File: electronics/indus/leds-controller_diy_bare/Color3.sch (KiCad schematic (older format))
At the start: 14 parts

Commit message: wip bare diy controller - dcdc and refactor
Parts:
- gave numbers to parts that had none: 14
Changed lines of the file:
@@
 $Descr A4 11693 8268
 encoding utf-8
-Sheet 5 8
+Sheet 5 9
 Title "Carte controlleur de LEDs 4 canaux"
 Date ""
@@
 VIN_24V
 $Comp
-L TPS92513 U?
+L TPS92513 U5
 U 1 1 5715946D
 P 5850 3550
-F 0 "U?" H 6200 2600 60  0000 C CNN
+F 0 "U5" H 6200 2600 60  0000 C CNN
 F 1 "TPS92513" H 5450 2600 60  0000 C CNN
 F 2 "" H 6000 3650 60  0000 C CNN
@@
 	1150 3450 5300 3450
 $Comp
-L GND-RESCUE-leds-controller #PWR?
+L GND-RESCUE-leds-controller #PWR020
 U 1 1 57159475
 P 3400 3100
-F 0 "#PWR?" H 3400 3100 30  0001 C CNN
+F 0 "#PWR020" H 3400 3100 30  0001 C CNN
 F 1 "GND" H 3400 3030 30  0001 C CNN
 F 2 "" H 3400 3100 60  0000 C CNN
@@
 $EndComp
 $Comp
-L C-RESCUE-leds-controller C?
+L C-RESCUE-leds-controller C20
 U 1 1 5715947B
 P 3400 2650
-F 0 "C?" H 3400 2750 40  0000 L CNN
+F 0 "C20" H 3400 2750 40  0000 L CNN
 F 1 "C" H 3406 2565 40  0000 L CNN
 F 2 "" H 3438 2500 30  0000 C CNN
@@
 $EndComp
 $Comp
-L R-RESCUE-leds-controller R?
+L R-RESCUE-leds-controller R23
 U 1 1 57159482
 P 4150 2700
-F 0 "R?" V 4230 2700 40  0000 C CNN
+F 0 "R23" V 4230 2700 40  0000 C CNN
 F 1 "R" V 4157 2701 40  0000 C CNN
 F 2 "" V 4080 2700 30  0000 C CNN
@@
 Connection ~ 4150 3450
 $Comp
-L C-RESCUE-leds-controller C?
+L C-RESCUE-leds-controller C18
 U 1 1 5715948C
 P 1650 4150
-F 0 "C?" H 1650 4250 40  0000 L CNN
+F 0 "C18" H 1650 4250 40  0000 L CNN
 F 1 "C" H 1656 4065 40  0000 L CNN
 F 2 "" H 1688 4000 30  0000 C CNN
@@
 Connection ~ 5800 4900
 $Comp
-L GND-RESCUE-leds-controller #PWR?
+L GND-RESCUE-leds-controller #PWR021
 U 1 1 5715949A
 P 6000 5250
-F 0 "#PWR?" H 6000 5250 30  0001 C CNN
+F 0 "#PWR021" H 6000 5250 30  0001 C CNN
 F 1 "GND" H 6000 5180 30  0001 C CNN
 F 2 "" H 6000 5250 60  0000 C CNN
@@
 Connection ~ 6000 4900
 $Comp
-L R-RESCUE-leds-controller R?
+L R-RESCUE-leds-controller R20
 U 1 1 571594A1
 P 2200 3800
-F 0 "R?" V 2280 3800 40  0000 C CNN
+F 0 "R20" V 2280 3800 40  0000 C CNN
 F 1 "R" V 2207 3801 40  0000 C CNN
 F 2 "" V 2130 3800 30  0000 C CNN
@@
 $EndComp
 $Comp
-L R-RESCUE-leds-controller R?
+L R-RESCUE-leds-controller R21
 U 1 1 571594A8
 P 2200 4500
-F 0 "R?" V 2280 4500 40  0000 C CNN
+F 0 "R21" V 2280 4500 40  0000 C CNN
 F 1 "R" V 2207 4501 40  0000 C CNN
 F 2 "" V 2130 4500 30  0000 C CNN
@@
 Connection ~ 2200 4150
 $Comp
-L C-RESCUE-leds-controller C?
+L C-RESCUE-leds-controller C19
 U 1 1 571594B8
 P 3100 4300
-F 0 "C?" H 3100 4400 40  0000 L CNN
+F 0 "C19" H 3100 4400 40  0000 L CNN
 F 1 "C" H 3106 4215 40  0000 L CNN
 F 2 "" H 3138 4150 30  0000 C CNN
@@
 $EndComp
 $Comp
-L R-RESCUE-leds-controller R?
+L R-RESCUE-leds-controller R22
 U 1 1 571594BF
 P 4100 4500
-F 0 "R?" V 4180 4500 40  0000 C CNN
+F 0 "R22" V 4180 4500 40  0000 C CNN
 F 1 "R" V 4107 4501 40  0000 C CNN
 F 2 "" V 4030 4500 30  0000 C CNN
@@
 Connection ~ 4100 4900
 $Comp
-L INDUCTOR L?
+L INDUCTOR L4
 U 1 1 571594CE
 P 8250 3450
-F 0 "L?" V 8200 3450 40  0000 C CNN
+F 0 "L4" V 8200 3450 40  0000 C CNN
 F 1 "XAL6060-153MEC - 15µH - 6A" V 8350 3450 40  0000 C CNN
 F 2 "risebox:SELF_COILCRAFT_XAL6060-153" H 8250 3450 60  0001 C CNN
@@
 	6050 2950 6050 2250
 $Comp
-L C-RESCUE-leds-controller C?
+L C-RESCUE-leds-controller C21
 U 1 1 571594DE
 P 6850 2900
-F 0 "C?" H 6850 3000 40  0000 L CNN
+F 0 "C21" H 6850 3000 40  0000 L CNN
 F 1 "C" H 6856 2815 40  0000 L CNN
 F 2 "" H 6888 2750 30  0000 C CNN
@@
 	8550 3450 10500 3450
 $Comp
-L C-RESCUE-leds-controller C?
+L C-RESCUE-leds-controller C22
 U 1 1 571594EF
 P 9600 3750
-F 0 "C?" H 9600 3850 40  0000 L CNN
+F 0 "C22" H 9600 3850 40  0000 L CNN
 F 1 "C" H 9606 3665 40  0000 L CNN
 F 2 "" H 9638 3600 30  0000 C CNN
@@
 Connection ~ 9600 4050
 $Comp
-L R-RESCUE-leds-controller R?
+L R-RESCUE-leds-controller R24
 U 1 1 571594FA
 P 8250 4050
-F 0 "R?" V 8330 4050 40  0000 C CNN
+F 0 "R24" V 8330 4050 40  0000 C CNN
 F 1 "R" V 8257 4051 40  0000 C CNN
 F 2 "" V 8180 4050 30  0000 C CNN
@@
 	8500 4050 10500 4050
 $Comp
-L R-RESCUE-leds-controller R?
+L R-RESCUE-leds-controller R25
 U 1 1 57159503
 P 10200 4500
-F 0 "R?" V 10280 4500 40  0000 C CNN
+F 0 "R25" V 10280 4500 40  0000 C CNN
 F 1 "R" V 10207 4501 40  0000 C CNN
 F 2 "" V 10130 4500 30  0000 C CNN
@@
 	10200 4900 10200 4750
 $Comp
-L DIODESCH D?
+L DIODESCH D5
 U 1 1 5715950D
 P 7400 4500
-F 0 "D?" H 7400 4600 40  0000 C CNN
+F 0 "D5" H 7400 4600 40  0000 C CNN
 F 1 "DIODESCH" H 7400 4400 40  0000 C CNN
 F 2 "" H 7400 4500 60  0000 C CNN

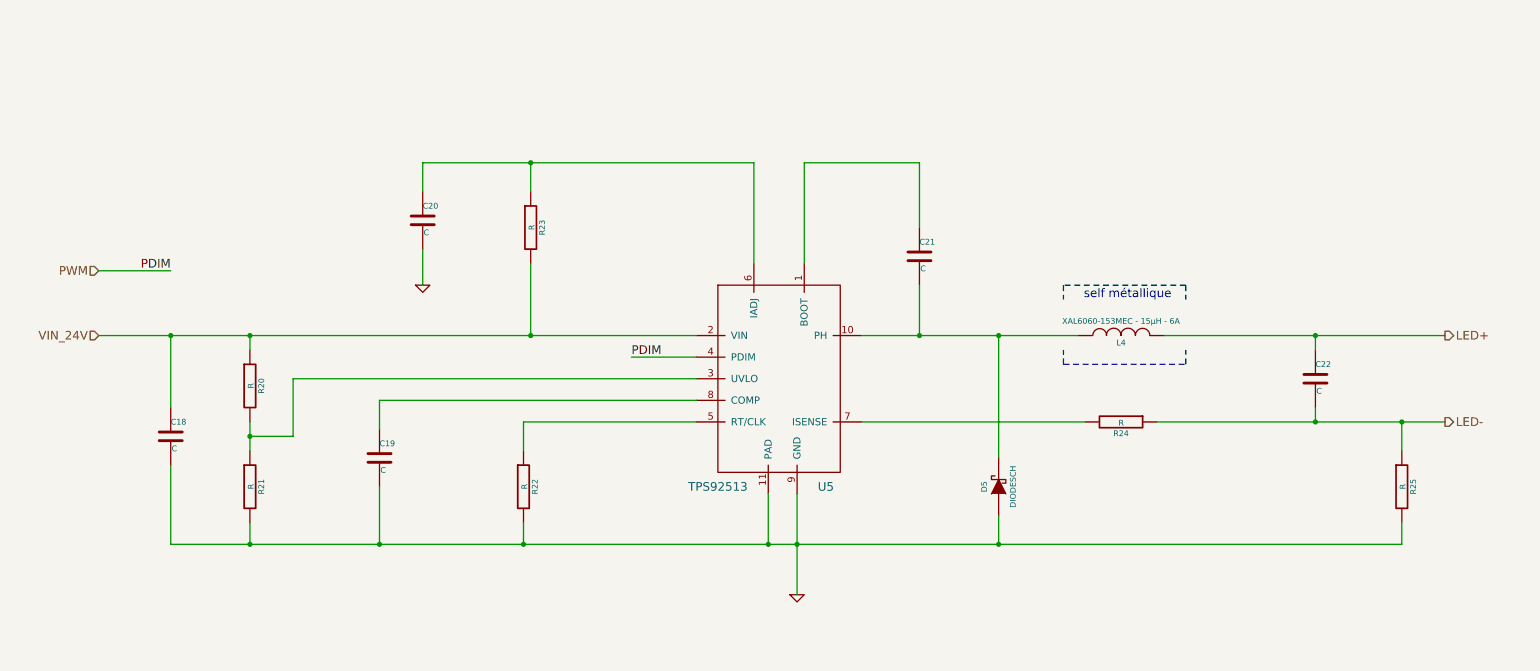
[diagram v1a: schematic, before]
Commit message: schema done - misses values
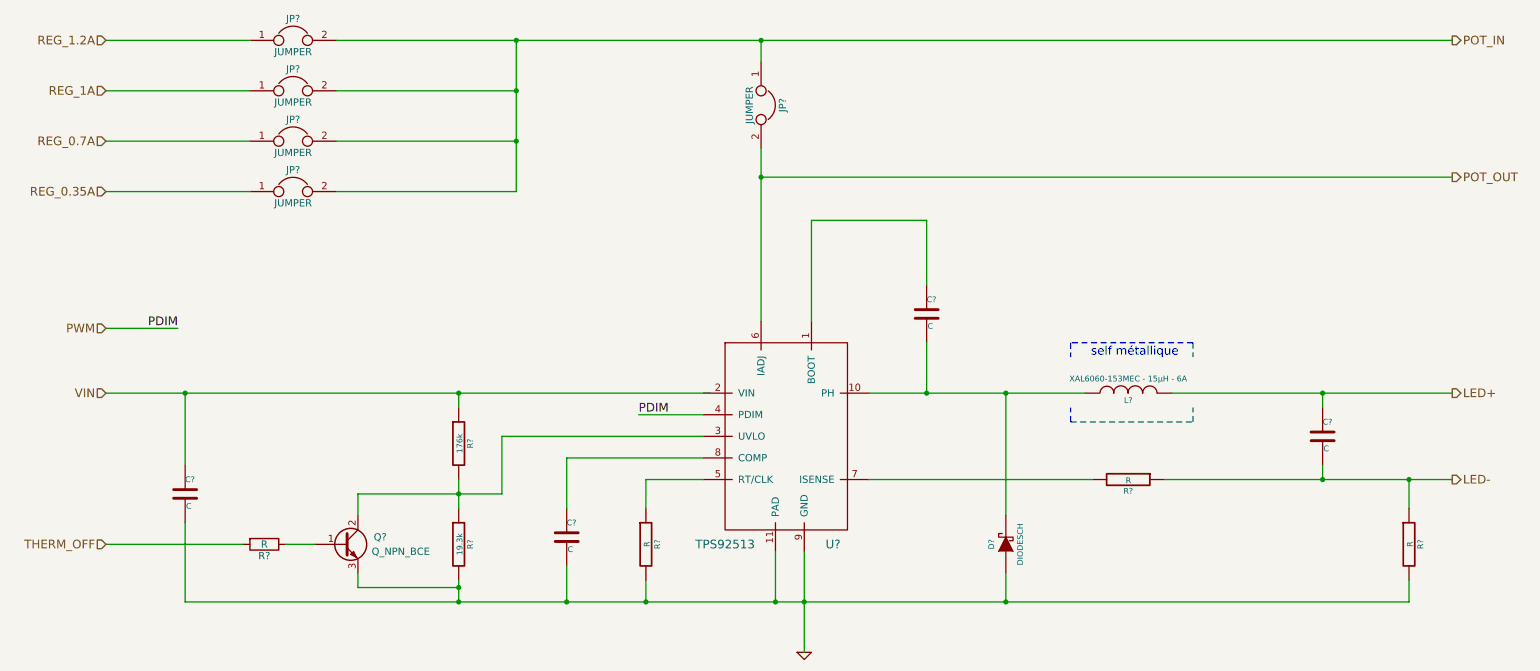
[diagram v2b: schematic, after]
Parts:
- removed C18, C19, C20, C21, C22: C, symbol C-RESCUE-leds-controller
- removed D5: DIODESCH, symbol DIODESCH
- removed L4: XAL6060-153MEC - 15µH - 6A, risebox:SELF_COILCRAFT_XAL6060-153, symbol INDUCTOR
- removed R20, R21, R22, R23, R24, R25: R, symbol R-RESCUE-leds-controller
- removed U5: TPS92513, symbol TPS92513
- added C? (x4): C, symbol C-RESCUE-leds-controller
- added D?: DIODESCH, symbol DIODESCH
- added JP? (x5): JUMPER, symbol JUMPER
- added L?: XAL6060-153MEC - 15µH - 6A, risebox:SELF_COILCRAFT_XAL6060-153, symbol INDUCTOR
- added Q?: Q_NPN_BCE, symbol Q_NPN_BCE
- added R?: 176k, symbol R-RESCUE-leds-controller
- added R?: 19.3k, symbol R-RESCUE-leds-controller
- added R? (x3): R, symbol R-RESCUE-leds-controller
- added R?: R, symbol R
- added U?: TPS92513, symbol TPS92513
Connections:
- net GND: now also C?.2, C?.2, D?.1 (A), Q?.3 (E), R?.2, R?.2, R?.2, U?.11 (PAD), U?.9 (GND)
- net LED+: now also C?.1, L?.2
- net LED-: now also C?.2, R?.1, R?.1
- net PWM: now also U?.4 (PDIM)
- new net: C?.1, U?.1 (BOOT)
- new net: C?.2, D?.2 (K), L?.1, U?.10 (PH)
- new net: Q?.2 (C), R?.1, R?.2, U?.3 (UVLO)
- new net: R?.1, U?.5 (RT/CLK)
- new net: R?.2, U?.7 (ISENSE)
- new net: C?.1, U?.8 (COMP)
- new net: Q?.1 (B), R?.1
- new net POT_IN: JP?.1, JP?.2, JP?.2, JP?.2, JP?.2
- new net POT_OUT: JP?.2, U?.6 (IADJ)
- new net REG_0.35A: JP?.1
- new net REG_0.7A: JP?.1
- new net REG_1.2A: JP?.1
- new net REG_1A: JP?.1
- new net THERM_OFF: R?.2
- new net VIN: C?.1, R?.1

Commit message: schema prctically ok missing refs
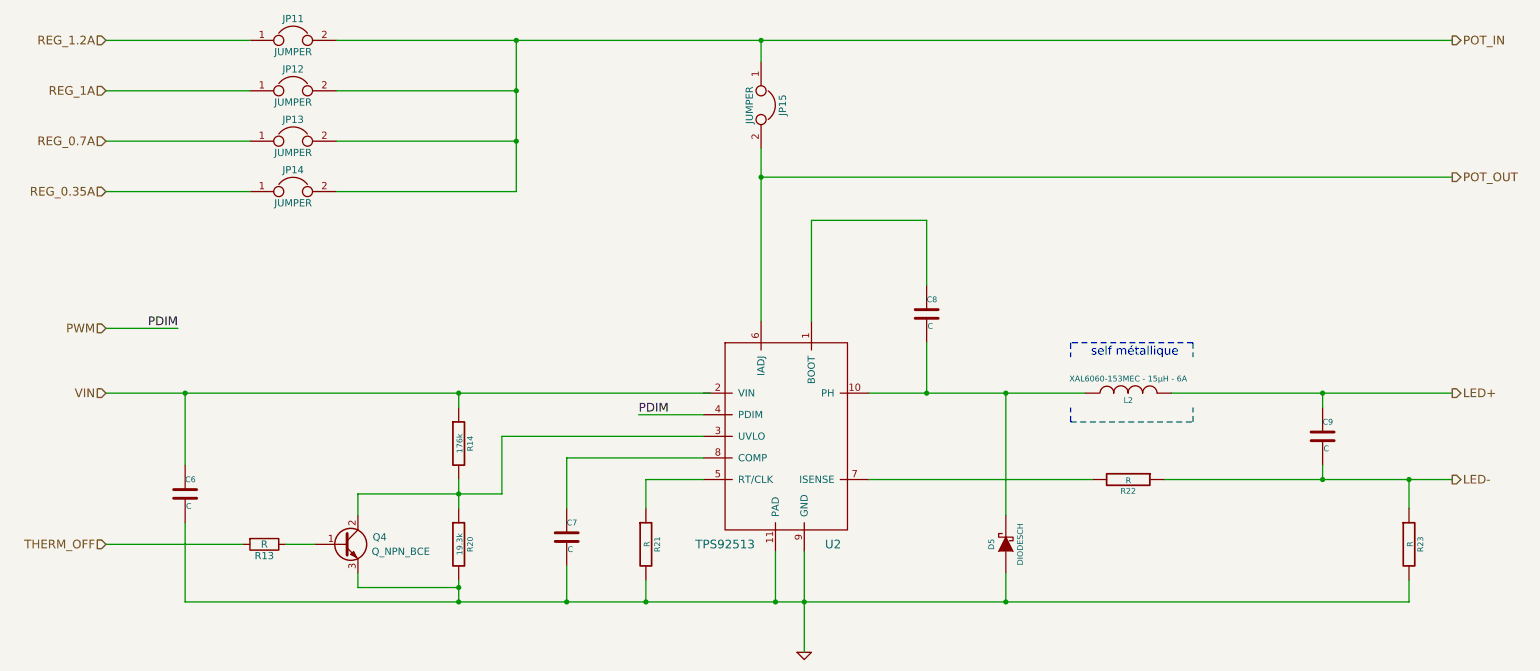
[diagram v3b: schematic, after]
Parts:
- gave numbers to parts that had none: 19
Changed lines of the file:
@@
 VIN
 $Comp
-L TPS92513 U?
+L TPS92513 U2
 U 1 1 5766F8DF
 P 5900 3950
-F 0 "U?" H 6250 3000 60  0000 C CNN
+F 0 "U2" H 6250 3000 60  0000 C CNN
 F 1 "TPS92513" H 5500 3000 60  0000 C CNN
 F 2 "" H 6050 4050 60  0000 C CNN
@@
 $EndComp
 $Comp
-L C-RESCUE-leds-controller C?
+L C-RESCUE-leds-controller C6
 U 1 1 5766F8E6
 P 1750 4550
-F 0 "C?" H 1750 4650 40  0000 L CNN
+F 0 "C6" H 1750 4650 40  0000 L CNN
 F 1 "C" H 1756 4465 40  0000 L CNN
 F 2 "" H 1788 4400 30  0000 C CNN
@@
 $EndComp
 $Comp
-L GND-RESCUE-leds-controller #PWR?
+L GND-RESCUE-leds-controller #PWR13
 U 1 1 5766F8ED
 P 6050 5650
-F 0 "#PWR?" H 6050 5650 30  0001 C CNN
+F 0 "#PWR13" H 6050 5650 30  0001 C CNN
 F 1 "GND" H 6050 5580 30  0001 C CNN
 F 2 "" H 6050 5650 60  0000 C CNN
@@
 $EndComp
 $Comp
-L R-RESCUE-leds-controller R?
+L R-RESCUE-leds-controller R14
 U 1 1 5766F8F3
 P 3650 4200
-F 0 "R?" V 3730 4200 40  0000 C CNN
+F 0 "R14" V 3730 4200 40  0000 C CNN
 F 1 "176k" V 3657 4201 40  0000 C CNN
 F 2 "" V 3580 4200 30  0000 C CNN
@@
 $EndComp
 $Comp
-L R-RESCUE-leds-controller R?
+L R-RESCUE-leds-controller R20
 U 1 1 5766F8FA
 P 3650 4900
-F 0 "R?" V 3730 4900 40  0000 C CNN
+F 0 "R20" V 3730 4900 40  0000 C CNN
 F 1 "19.3k" V 3657 4901 40  0000 C CNN
 F 2 "" V 3580 4900 30  0000 C CNN
@@
 $EndComp
 $Comp
-L C-RESCUE-leds-controller C?
+L C-RESCUE-leds-controller C7
 U 1 1 5766F901
 P 4400 4850
-F 0 "C?" H 4400 4950 40  0000 L CNN
+F 0 "C7" H 4400 4950 40  0000 L CNN
 F 1 "C" H 4406 4765 40  0000 L CNN
 F 2 "" H 4438 4700 30  0000 C CNN
@@
 $EndComp
 $Comp
-L R-RESCUE-leds-controller R?
+L R-RESCUE-leds-controller R21
 U 1 1 5766F908
 P 4950 4900
-F 0 "R?" V 5030 4900 40  0000 C CNN
+F 0 "R21" V 5030 4900 40  0000 C CNN
 F 1 "R" V 4957 4901 40  0000 C CNN
 F 2 "" V 4880 4900 30  0000 C CNN
@@
 $EndComp
 $Comp
-L INDUCTOR L?
+L INDUCTOR L2
 U 1 1 5766F90F
 P 8300 3850
-F 0 "L?" V 8250 3850 40  0000 C CNN
+F 0 "L2" V 8250 3850 40  0000 C CNN
 F 1 "XAL6060-153MEC - 15µH - 6A" V 8400 3850 40  0000 C CNN
 F 2 "risebox:SELF_COILCRAFT_XAL6060-153" H 8300 3850 60  0001 C CNN
@@
 self métallique
 $Comp
-L C-RESCUE-leds-controller C?
+L C-RESCUE-leds-controller C8
 U 1 1 5766F917
 P 6900 3300
-F 0 "C?" H 6900 3400 40  0000 L CNN
+F 0 "C8" H 6900 3400 40  0000 L CNN
 F 1 "C" H 6906 3215 40  0000 L CNN
 F 2 "" H 6938 3150 30  0000 C CNN
@@
 $EndComp
 $Comp
-L C-RESCUE-leds-controller C?
+L C-RESCUE-leds-controller C9
 U 1 1 5766F91E
 P 9650 4150
-F 0 "C?" H 9650 4250 40  0000 L CNN
+F 0 "C9" H 9650 4250 40  0000 L CNN
 F 1 "C" H 9656 4065 40  0000 L CNN
 F 2 "" H 9688 4000 30  0000 C CNN
@@
 $EndComp
 $Comp
-L R-RESCUE-leds-controller R?
+L R-RESCUE-leds-controller R22
 U 1 1 5766F925
 P 8300 4450
-F 0 "R?" V 8380 4450 40  0000 C CNN
+F 0 "R22" V 8380 4450 40  0000 C CNN
 F 1 "R" V 8307 4451 40  0000 C CNN
 F 2 "" V 8230 4450 30  0000 C CNN
@@
 $EndComp
 $Comp
-L R-RESCUE-leds-controller R?
+L R-RESCUE-leds-controller R23
 U 1 1 5766F92C
 P 10250 4900
-F 0 "R?" V 10330 4900 40  0000 C CNN
+F 0 "R23" V 10330 4900 40  0000 C CNN
 F 1 "R" V 10257 4901 40  0000 C CNN
 F 2 "" V 10180 4900 30  0000 C CNN
@@
 $EndComp
 $Comp
-L DIODESCH D?
+L DIODESCH D5
 U 1 1 5766F933
 P 7450 4900
-F 0 "D?" H 7450 5000 40  0000 C CNN
+F 0 "D5" H 7450 5000 40  0000 C CNN
 F 1 "DIODESCH" H 7450 4800 40  0000 C CNN
 F 2 "" H 7450 4900 60  0000 C CNN
@@
 PDIM
 $Comp
-L JUMPER JP?
+L JUMPER JP11
 U 1 1 5766F93D
 P 2500 1400
-F 0 "JP?" H 2500 1550 50  0000 C CNN
+F 0 "JP11" H 2500 1550 50  0000 C CNN
 F 1 "JUMPER" H 2500 1320 50  0000 C CNN
 F 2 "" H 2500 1400 50  0000 C CNN
@@
 $EndComp
 $Comp
-L JUMPER JP?
+L JUMPER JP12
 U 1 1 5766F944
 P 2500 1750
-F 0 "JP?" H 2500 1900 50  0000 C CNN
+F 0 "JP12" H 2500 1900 50  0000 C CNN
 F 1 "JUMPER" H 2500 1670 50  0000 C CNN
 F 2 "" H 2500 1750 50  0000 C CNN
@@
 $EndComp
 $Comp
-L JUMPER JP?
+L JUMPER JP13
 U 1 1 5766F94B
 P 2500 2100
-F 0 "JP?" H 2500 2250 50  0000 C CNN
+F 0 "JP13" H 2500 2250 50  0000 C CNN
 F 1 "JUMPER" H 2500 2020 50  0000 C CNN
 F 2 "" H 2500 2100 50  0000 C CNN
@@
 $EndComp
 $Comp
-L JUMPER JP?
+L JUMPER JP14
 U 1 1 5766F952
 P 2500 2450
-F 0 "JP?" H 2500 2600 50  0000 C CNN
+F 0 "JP14" H 2500 2600 50  0000 C CNN
 F 1 "JUMPER" H 2500 2370 50  0000 C CNN
 F 2 "" H 2500 2450 50  0000 C CNN
@@
 REG_0.35A
 $Comp
-L JUMPER JP?
+L JUMPER JP15
 U 1 1 5766F95D
 P 5750 1850
-F 0 "JP?" H 5750 2000 50  0000 C CNN
+F 0 "JP15" H 5750 2000 50  0000 C CNN
 F 1 "JUMPER" H 5750 1770 50  0000 C CNN
 F 2 "" H 5750 1850 50  0000 C CNN
@@
 Connection ~ 3650 5200
 $Comp
-L Q_NPN_BCE Q?
+L Q_NPN_BCE Q4
 U 1 1 5766F9C8
 P 2850 4900
-F 0 "Q?" H 3150 4950 50  0000 R CNN
+F 0 "Q4" H 3150 4950 50  0000 R CNN
 F 1 "Q_NPN_BCE" H 3450 4850 50  0000 R CNN
 F 2 "" H 3050 5000 50  0000 C CNN
@@
 THERM_OFF
 $Comp
-L R R?
+L R R13
 U 1 1 5766F9D0
 P 2300 4900
-F 0 "R?" V 2380 4900 50  0000 C CNN
+F 0 "R13" V 2380 4900 50  0000 C CNN
 F 1 "R" V 2300 4900 50  0000 C CNN
 F 2 "" V 2230 4900 50  0000 C CNN

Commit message: Added missing Capa & Resistor values
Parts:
- added C23: 4.7µF, symbol C
- C6, C9: value C -> 4.7µF
- C7, C8: value C -> 0.1µF
- R21: value R -> 200k
- R23: value R -> 0.2
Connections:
- net GND: now also C23.2
- net VIN: now also C23.1
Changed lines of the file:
@@
 P 1750 4550
 F 0 "C6" H 1750 4650 40  0000 L CNN
-F 1 "C" H 1756 4465 40  0000 L CNN
+F 1 "4.7µF" H 1756 4465 40  0000 L CNN
 F 2 "" H 1788 4400 30  0000 C CNN
 F 3 "" H 1750 4550 60  0000 C CNN
@@
 P 4400 4850
 F 0 "C7" H 4400 4950 40  0000 L CNN
-F 1 "C" H 4406 4765 40  0000 L CNN
+F 1 "0.1µF" H 4406 4765 40  0000 L CNN
 F 2 "" H 4438 4700 30  0000 C CNN
 F 3 "" H 4400 4850 60  0000 C CNN
@@
 P 4950 4900
 F 0 "R21" V 5030 4900 40  0000 C CNN
-F 1 "R" V 4957 4901 40  0000 C CNN
+F 1 "200k" V 4957 4901 40  0000 C CNN
 F 2 "" V 4880 4900 30  0000 C CNN
 F 3 "" H 4950 4900 30  0000 C CNN
@@
 P 6900 3300
 F 0 "C8" H 6900 3400 40  0000 L CNN
-F 1 "C" H 6906 3215 40  0000 L CNN
+F 1 "0.1µF" H 6906 3215 40  0000 L CNN
 F 2 "" H 6938 3150 30  0000 C CNN
 F 3 "" H 6900 3300 60  0000 C CNN
@@
 P 9650 4150
 F 0 "C9" H 9650 4250 40  0000 L CNN
-F 1 "C" H 9656 4065 40  0000 L CNN
+F 1 "4.7µF" H 9656 4065 40  0000 L CNN
 F 2 "" H 9688 4000 30  0000 C CNN
 F 3 "" H 9650 4150 60  0000 C CNN
@@
 P 10250 4900
 F 0 "R23" V 10330 4900 40  0000 C CNN
-F 1 "R" V 10257 4901 40  0000 C CNN
+F 1 "0.2" V 10257 4901 40  0000 C CNN
 F 2 "" V 10180 4900 30  0000 C CNN
 F 3 "" H 10250 4900 30  0000 C CNN
@@
 POT_OUT
 Wire Wire Line
-	1200 3850 1750 3850
-Wire Wire Line
-	1750 3850 3650 3850
-Wire Wire Line
-	3650 3850 3650 3850
-Wire Wire Line
-	3650 3850 5400 3850
-Wire Wire Line
-	1750 5300 3650 5300
-Wire Wire Line
-	3650 5300 4400 5300
-Wire Wire Line
-	4400 5300 4950 5300
-Wire Wire Line
-	4950 5300 5850 5300
-Wire Wire Line
-	5850 5300 6050 5300
-Wire Wire Line
-	6050 5300 7450 5300
-Wire Wire Line
-	7450 5300 10250 5300
-Wire Wire Line
-	6050 4950 6050 5300
-Wire Wire Line
-	6050 5300 6050 5650
+	1200 3850 5400 3850
+Wire Wire Line
+	1750 5300 10250 5300
+Wire Wire Line
+	6050 4950 6050 5650
 Wire Wire Line
 	5850 4950 5850 5300
@@
 Connection ~ 6050 5300
 Wire Wire Line
-	3650 4450 3650 4550
-Wire Wire Line
-	3650 4550 3650 4650
+	3650 4450 3650 4650
 Wire Wire Line
 	3950 4550 3950 4150
@@
 	8750 3500 8750 3600
 Wire Wire Line
-	6500 3850 6900 3850
-Wire Wire Line
-	6900 3850 7450 3850
-Wire Wire Line
-	7450 3850 8000 3850
+	6500 3850 8000 3850
 Wire Wire Line
 	6100 3350 6100 2650
@@
 Connection ~ 6900 3850
 Wire Wire Line
-	8600 3850 9650 3850
-Wire Wire Line
-	9650 3850 10550 3850
+	8600 3850 10550 3850
 Wire Wire Line
 	9650 3950 9650 3850
@@
 	6500 4450 8050 4450
 Wire Wire Line
-	8550 4450 9650 4450
-Wire Wire Line
-	9650 4450 10250 4450
-Wire Wire Line
-	10250 4450 10550 4450
+	8550 4450 10550 4450
 Wire Wire Line
 	10250 4650 10250 4450
@@
 	1200 2450 2200 2450
 Wire Wire Line
-	2800 1400 4050 1400
-Wire Wire Line
-	4050 1400 5750 1400
-Wire Wire Line
-	5750 1400 10550 1400
+	2800 1400 10550 1400
 Wire Wire Line
 	2800 1750 4050 1750
 Wire Wire Line
-	4050 1400 4050 1750
-Wire Wire Line
-	4050 1750 4050 2100
-Wire Wire Line
-	4050 2100 4050 2450
+	4050 1400 4050 2450
 Connection ~ 4050 1400
 Wire Wire Line
@@
 Connection ~ 5750 2350
 Wire Wire Line
-	5750 2150 5750 2350
-Wire Wire Line
-	5750 2350 5750 3350
+	5750 2150 5750 3350
 Wire Wire Line
 	5750 1550 5750 1400
@@
 	1750 4750 1750 5300
 Wire Wire Line
-	3650 5150 3650 5200
-Wire Wire Line
-	3650 5200 3650 5300
+	3650 5150 3650 5300
 Wire Wire Line
 	3650 3950 3650 3850
@@
 	2950 4700 2950 4550
 Wire Wire Line
-	2950 4550 3650 4550
-Wire Wire Line
-	3650 4550 3950 4550
+	2950 4550 3950 4550
 Wire Wire Line
 	2950 5100 2950 5200
@@
 Wire Wire Line
 	2150 4900 1200 4900
+$Comp
+L C C23
+U 1 1 576AB9EE
+P 2050 4550
+F 0 "C23" H 2075 4650 50  0000 L CNN
+F 1 "4.7µF" H 2075 4450 50  0000 L CNN
+F 2 "" H 2088 4400 50  0000 C CNN
+F 3 "" H 2050 4550 50  0000 C CNN
+	1    2050 4550
+	1    0    0    -1
+$EndComp
+Wire Wire Line
+	2050 4400 2050 3850
+Connection ~ 2050 3850
+Wire Wire Line
+	2050 4700 2050 5300
+Connection ~ 2050 5300
 $EndSCHEMATC
